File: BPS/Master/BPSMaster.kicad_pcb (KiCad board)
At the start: 2 copper layers, 100 x 75 mm, 180 parts, among them J1 SWD, J10 DisplayJumper, J11 FrontFans, J12 BackFans, J13 ErrorLightConnector, J14 Conn_01x03, J2 Logic Analyzer, J3 CurrentSlaveConnector, J4 CarPowerConnector, J5 CAN_Out, J6 ContactorConnector, J7 VoltageSlaveConnector, J8 DisplayConnector, J9 TempSlaveConnector, Q1 VND5N07-E, Q2 NVR4003NT3G, Q3 NVR4003NT3G, Q4 NVR4003NT3G, SW1 B3SL-1002P, U1 STM32F413RHTx, U10 LTC6820, U11 HX1188FNL, U12 LTC6820, U13 Si8641EC-B-IS1, U14 SI8660EC-B-IS1, U15 RI3-1205S, U16 SI8261ABC-IS, U2 RI3-1205S, U3 NCP1117-3.3_SOT223, U4 CDSOT23-T24CAN, U5 ADM3055E, U6 BAS70-04, U7 SI8261ABC-IS, U8 M24128, Y1 NX8045GB-8.000M-STD-CSJ-1

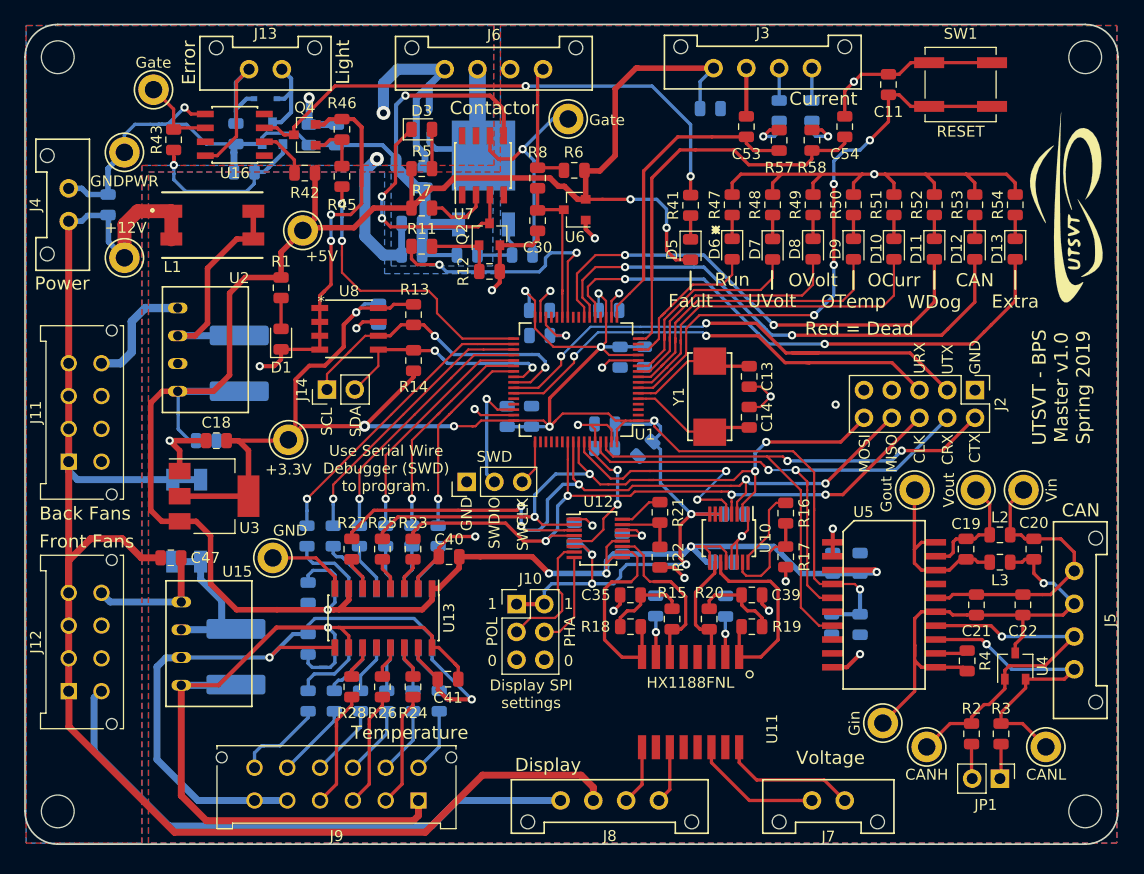
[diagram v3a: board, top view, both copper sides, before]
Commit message: Adds master board v1.1.
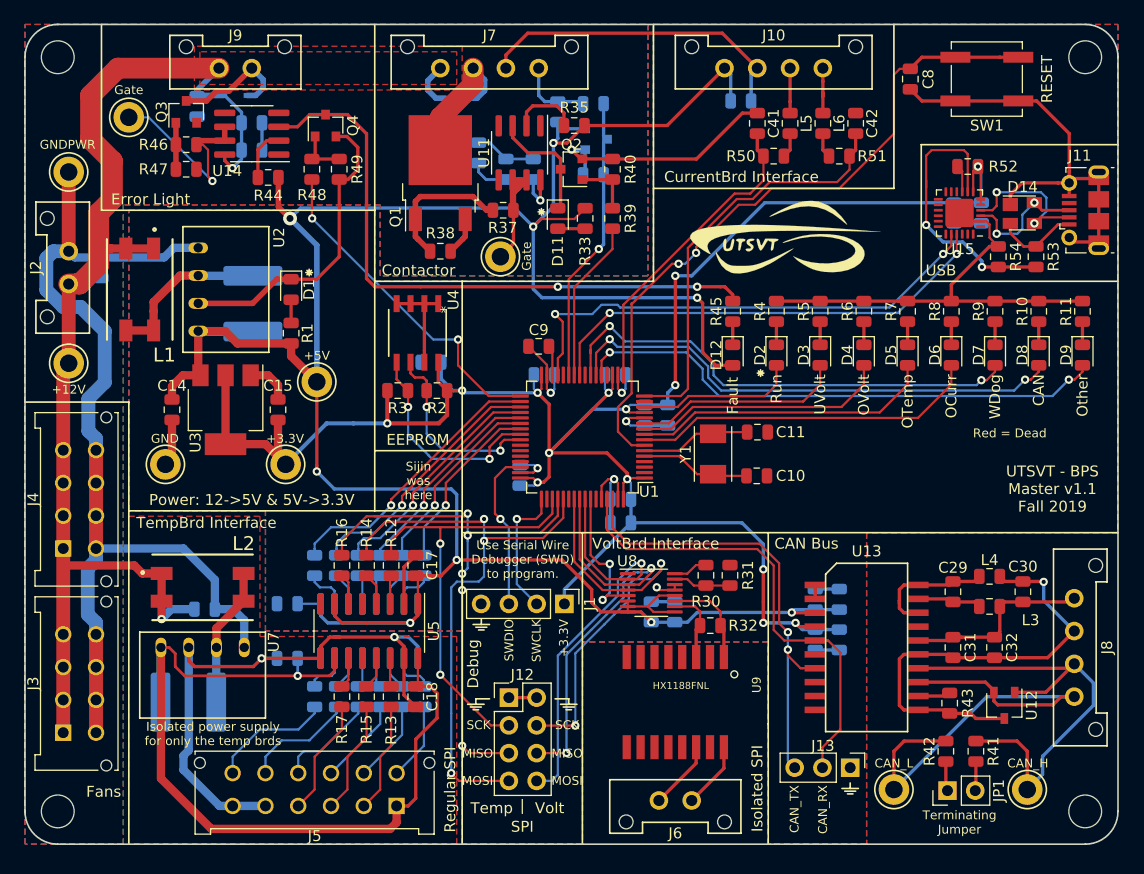
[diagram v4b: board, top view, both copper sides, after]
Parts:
- removed C45, C50: 0.1uF, Capacitor_SMD:C_0805_2012Metric
- removed C46: 470pF, Capacitor_SMD:C_2220_5650Metric
- removed C47: 4.7uF, Capacitor_SMD:C_0805_2012Metric
- removed C48, C53, C54: 1uF, Capacitor_SMD:C_0805_2012Metric
- removed C49: 10uF, Capacitor_SMD:C_0805_2012Metric
- removed J14: Conn_01x03, Connector_PinHeader_2.54mm:PinHeader_1x02_P2.54mm_Vertical
- removed R57, R58: 220k, Resistor_SMD:R_0805_2012Metric
- removed TP12: CAN_L, TestPoint:TestPoint_Keystone_5005-5009_Compact
- removed TP13: ContactorGate_TP, TestPoint:TestPoint_Keystone_5005-5009_Compact
- removed TP14: StrobeLightGate_TP, TestPoint:TestPoint_Keystone_5005-5009_Compact
- removed TP15: GNDPWR_TP, TestPoint:TestPoint_Keystone_5005-5009_Compact
- removed U16: SI8261ABC-IS, Package_SO:SOIC-8_3.9x4.9mm_P1.27mm
- added C32: 0.01uF, Capacitor_SMD:C_0805_2012Metric, F.Cu at (188.7, 132.0)
- added C33: 10uF, Capacitor_SMD:C_0805_2012Metric, B.Cu at (174.5, 127.6)
- added D14: SP0503BAHT, Package_TO_SOT_SMD:SOT-143, F.Cu at (191.2, 92.2)
- added U9: HX1188FNL, UTSVT_BPS:HXXXX, F.Cu at (159.5, 137.0)
- C10: value 1uF -> 6pF; moved to F.Cu
- C11: value 0.1uF -> 6pF
- C12: value 0.1uF -> 470pF; footprint Capacitor_SMD:C_0805_2012Metric -> Capacitor_SMD:C_2220_5650Metric
- C13: value 6pF -> 4.7uF; moved to B.Cu
- C14: value 6pF -> 10uF
- C15: value 470pF -> 10uF; footprint Capacitor_SMD:C_2220_5650Metric -> Capacitor_SMD:C_0805_2012Metric; moved to F.Cu
- C16: value 4.7uF -> 0.1uF
- C17: value 0.1uF -> 0.1u; moved to F.Cu
- C18: value 10uF -> 0.1u
- C19: value 10uF -> 0.1u; moved to B.Cu
- C20: value 0.22uF -> 0.1u; moved to B.Cu
- C21: value 0.1uF -> 470p; footprint Capacitor_SMD:C_0805_2012Metric -> Capacitor_SMD:C_2220_5650Metric; moved to B.Cu
- C22: value 0.01uF -> 4.7u; moved to B.Cu
- C23: value 10uF -> 0.1uF
- C25: value 0.1uF -> 1u
- C26: value 0.01uF -> 10u
- C27: value 1uF -> 0.1u
- C28: value 10uF -> 1u
- C29: value 0.1uF -> 0.22uF; moved to F.Cu
- C30: value 1uF -> 10uF
- C31, L5, L6, Q1: moved to F.Cu
- C34: value 0.01uF -> 0.1uF
- C35, C39: value 0.01uF -> 0.1uF; moved to B.Cu
- C36: value 0.1uF -> 0.01uF
- C37: value 0.01uF -> 1uF
- C38: value 0.1uF -> 10uF
- C40, R23, R24, R25, R26, R27, R28: moved to B.Cu
- C41: value 0.1uF -> 1uF
- C42: value 0.1uF -> 1uF; moved to F.Cu
- C43, C5: value 0.1uF -> 4.7uF
- C7: value 4.7uF -> 1uF
- C8: value 2.2uF -> 0.1uF; moved to F.Cu
- C9: value 0.1uF -> 2.2uF; moved to F.Cu
- D10: value OCurr -> 1N4148WS; footprint LED_SMD:LED_0805_2012Metric -> Diode_SMD:D_SOD-323; moved to B.Cu
- D11: value WDError -> ContactorEn
- D12: value CANError -> Fault
- D13: value Extra -> 1N4148WS; footprint LED_SMD:LED_0805_2012Metric -> Diode_SMD:D_SOD-323; moved to B.Cu
- D2: value 1N4148WS -> Heartbeat; footprint Diode_SMD:D_SOD-323 -> LED_SMD:LED_0805_2012Metric; moved to F.Cu
- D3: value ContactorEn -> UVolt
- D4: value 1N4148WS -> OVolt; footprint Diode_SMD:D_SOD-323 -> LED_SMD:LED_0805_2012Metric; moved to F.Cu
- D5: value Fault -> OTemp
- D6: value Heartbeat -> OCurr
- D7: value UVolt -> WDError
- D8: value OVolt -> CANError
- D9: value OTemp -> Extra
- J1: footprint Connector_PinHeader_2.54mm:PinHeader_1x03_P2.54mm_Vertical -> Connector_PinHeader_2.54mm:PinHeader_1x04_P2.54mm_Vertical
- J10: value DisplayJumper -> CurrentSlaveConnector; footprint Connector_PinHeader_2.54mm:PinHeader_2x03_P2.54mm_Vertical -> UTSVT_Connectors:Molex_MicroFit3.0_1x4xP3.00mm_PolarizingPeg_Vertical
- J11: value FrontFans -> USB_B_Micro; footprint UTSVT_Connectors:Molex_MicroFit3.0_2x4xP3.00mm_PolarizingPeg_Vertical -> Connector_USB:USB_Micro-B_Molex-105017-0001
- J12: value BackFans -> Logic Analyzer; footprint UTSVT_Connectors:Molex_MicroFit3.0_2x4xP3.00mm_PolarizingPeg_Vertical -> Connector_PinHeader_2.54mm:PinHeader_2x04_P2.54mm_Vertical
- J13: value ErrorLightConnector -> CAN Analyzer; footprint UTSVT_Connectors:Molex_MicroFit3.0_1x2xP3.00mm_PolarizingPeg_Vertical -> Connector_PinHeader_2.54mm:PinHeader_1x03_P2.54mm_Vertical
- J2: value Logic Analyzer -> CarPowerConnector; footprint Connector_PinHeader_2.54mm:PinHeader_2x05_P2.54mm_Vertical -> UTSVT_Connectors:Molex_MicroFit3.0_1x2xP3.00mm_PolarizingPeg_Vertical
- J3: value CurrentSlaveConnector -> FrontFans; footprint UTSVT_Connectors:Molex_MicroFit3.0_1x4xP3.00mm_PolarizingPeg_Vertical -> UTSVT_Connectors:Molex_MicroFit3.0_2x4xP3.00mm_PolarizingPeg_Vertical
- J4: value CarPowerConnector -> BackFans; footprint UTSVT_Connectors:Molex_MicroFit3.0_1x2xP3.00mm_PolarizingPeg_Vertical -> UTSVT_Connectors:Molex_MicroFit3.0_2x4xP3.00mm_PolarizingPeg_Vertical
- J5: value CAN_Out -> TempSlaveConnector; footprint UTSVT_Connectors:Molex_MicroFit3.0_1x4xP3.00mm_PolarizingPeg_Vertical -> UTSVT_Connectors:Molex_MicroFit3.0_2x6xP3.00mm_PolarizingPeg_Vertical
- J6: value ContactorConnector -> VoltageSlaveConnector; footprint UTSVT_Connectors:Molex_MicroFit3.0_1x4xP3.00mm_PolarizingPeg_Vertical -> UTSVT_Connectors:Molex_MicroFit3.0_1x2xP3.00mm_PolarizingPeg_Vertical
- J7: value VoltageSlaveConnector -> ContactorConnector; footprint UTSVT_Connectors:Molex_MicroFit3.0_1x2xP3.00mm_PolarizingPeg_Vertical -> UTSVT_Connectors:Molex_MicroFit3.0_1x4xP3.00mm_PolarizingPeg_Vertical
- J8: value DisplayConnector -> CAN_Out
- J9: value TempSlaveConnector -> ErrorLightConnector; footprint UTSVT_Connectors:Molex_MicroFit3.0_2x6xP3.00mm_PolarizingPeg_Vertical -> UTSVT_Connectors:Molex_MicroFit3.0_1x2xP3.00mm_PolarizingPeg_Vertical
- L2: value 2kH -> 10u; footprint Inductor_SMD:L_0805_2012Metric -> UTSVT_BPS:SRF0905A
- L4: value 10uH -> 2kH; footprint UTSVT_BPS:SRF0905A -> Inductor_SMD:L_0805_2012Metric; moved to F.Cu
- Q2, Q4: value NVR4003NT3G -> NTR4003NT1G
- Q3: value NVR4003NT3G -> NTR4003NT1G; moved to F.Cu
- R10: value 100k -> 750; moved to F.Cu
- R11: value 0 -> 750
- R12: value 100k -> 50
- R13, R14: value 4.7k -> 50
- R15: value 49.9 -> 50
- R16: value 806 -> 50
- R17: value 1.21k -> 50
- R18, R19, R20: value 49.9 -> 50; moved to B.Cu
- R2, R3: value 60 -> 4.7k
- R21: value 806 -> 50; moved to B.Cu
- R22: value 1.21k -> 50; moved to B.Cu
- R30: value 50 -> 806; moved to F.Cu
- R31: value 50 -> 1.21k; moved to F.Cu
- R32: value 50 -> 120; moved to F.Cu
- R33: value 50 -> 1.5k; moved to F.Cu
- R34: value 50 -> 4.7k
- R35: value 50 -> 470; moved to F.Cu
- R36: value 50 -> 1k
- R37, R39: value 50 -> 0; moved to F.Cu
- R38, R40: value 50 -> 10k; moved to F.Cu
- R4: value 0 -> 680
- R41: value 1.6k -> 60
- R42: value 470 -> 60
- R44: value 100k -> 470; moved to F.Cu
- R45: value 0 -> 1.6k
- R46: value 100k -> 0
- R47: value 680 -> 10k
- R48: value 750 -> 0
- R49: value 750 -> 10k
- R5: value 1.5k -> 750
- R50, R51: value 750 -> 220k
- R52: value 750 -> 1k
- R53: value 750 -> 22.1k
- R54: value 750 -> 47.5k
- R6: value 4.7k -> 750
- R7: value 470 -> 750
- R8: value 1k -> 750
- R9: value 0 -> 750; moved to F.Cu
- TP3: value GND_TP -> GNDPWR_TP
- TP4: value +3.3V_TP -> GND_TP
- TP5: value CAN_ISO_Vout -> +3.3V_TP
- TP6: value CAN_ISO_Vin -> ContactorGate_TP
- TP7: value CAN_ISO_GndIn -> CAN_H
- TP8: value CAN_ISO_GndOut -> CAN_L
- TP9: value CAN_H -> StrobeLightGate_TP
- U10: value LTC6820 -> BAS70-04; footprint Package_SO:MSOP-16_3x4mm_P0.5mm -> Package_TO_SOT_SMD:SOT-23; moved to B.Cu
- U11: value HX1188FNL -> SI8261ABC-IS; footprint UTSVT_BPS:HXXXX -> Package_SO:SOIC-8_3.9x4.9mm_P1.27mm
- U12: value LTC6820 -> CDSOT23-T24CAN; footprint Package_SO:MSOP-16_3x4mm_P0.5mm -> Package_TO_SOT_SMD:SOT-23W
- U13: value Si8641EC-B-IS1 -> ADM3055E; footprint Package_SO:SOIC-16_3.9x9.9mm_P1.27mm -> UTSVT_ICs:SOIC-20W_7.5x15.4mm_Pitch1.27mm
- U14: value SI8660EC-B-IS1 -> SI8261ABC-IS; footprint Package_SO:SOIC-16_3.9x9.9mm_P1.27mm -> Package_SO:SOIC-8_3.9x4.9mm_P1.27mm; moved to F.Cu
- U15: value RI3-1205S -> CP2102N-A01-GQFN24; footprint UTSVT_ICs:RI3_DC_Converter -> Package_DFN_QFN:QFN-24-1EP_4x4mm_P0.5mm_EP2.6x2.6mm
- U4: value CDSOT23-T24CAN -> M24128; footprint Package_TO_SOT_SMD:SOT-23W -> UTSVT_BPS:M24128-BRMN6P
- U5: value ADM3055E -> Si8641EC-B-IS1; footprint UTSVT_ICs:SOIC-20W_7.5x15.4mm_Pitch1.27mm -> Package_SO:SOIC-16_3.9x9.9mm_P1.27mm
- U6: value BAS70-04 -> SI8660EC-B-IS1; footprint Package_TO_SOT_SMD:SOT-23 -> Package_SO:SOIC-16_3.9x9.9mm_P1.27mm; moved to B.Cu
- U7: value SI8261ABC-IS -> RI3-1205S; footprint Package_SO:SOIC-8_3.9x4.9mm_P1.27mm -> UTSVT_ICs:RI3_DC_Converter
- U8: value M24128 -> LTC6820; footprint UTSVT_BPS:M24128-BRMN6P -> Package_SO:MSOP-16_3x4mm_P0.5mm
- Y1: value NX8045GB-8.000M-STD-CSJ-1 -> 8M; footprint UTSVT_BPS:NX8045GB-8.000M-STD-CSJ-1 -> Crystal:Crystal_SMD_TXC_7A-2Pin_5x3.2mm
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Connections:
- C10 pad 1: +3V3 -> /OSC_IN
- C11 pad 1: /NRST -> /OSC_OUT
- C12 pad 1: GND -> Net-(C12-Pad1)
- C13 pad 1: /OSC_OUT -> +12V
- C13 pad 2: GND -> GNDPWR
- C14 pad 1: /OSC_IN -> +5V
- C15 pad 1: Net-(C15-Pad1) -> +3V3
- C15 pad 2: +5V -> GND
- C16 pad 1: +12V -> +3V3
- C16 pad 2: GNDPWR -> GND
- C18 pad 1: +3V3 -> +5VL
- C18 pad 2: GND -> GND_A
- C19 pad 1: Net-(C19-Pad1) -> +5V
- C19 pad 2: Net-(C19-Pad2) -> GND
- C20 pad 1: Net-(C20-Pad1) -> +5VL
- C20 pad 2: Net-(C20-Pad2) -> GND_A
- C21 pad 1: Net-(C20-Pad1) -> Net-(C21-Pad1)
- C21 pad 2: Net-(C20-Pad2) -> +5VL
- C22 pad 1: Net-(C20-Pad1) -> +12V
- C22 pad 2: Net-(C20-Pad2) -> GNDPWR
- C25 pad 1: +3V3 -> GNDPWR
- C25 pad 2: GND -> +12V
- C26 pad 1: +3V3 -> +12V
- C26 pad 2: GND -> GNDPWR
- C27 pad 1: GNDPWR -> +12V
- C27 pad 2: +12V -> GNDPWR
- C28 pad 1: +12V -> /PB1
- C28 pad 2: GNDPWR -> GND
- C29 pad 1: +12V -> Net-(C29-Pad1)
- C29 pad 2: GNDPWR -> Net-(C29-Pad2)
- C30 pad 1: /PB1 -> Net-(C30-Pad1)
- C30 pad 2: GND -> Net-(C30-Pad2)
- C31 pad 1: +3V3 -> Net-(C30-Pad1)
- C31 pad 2: GND -> Net-(C30-Pad2)
- C34 pad 1: Net-(C34-Pad1) -> +5V
- C35 pad 1: Net-(C35-Pad1) -> +3V3
- C37 pad 1: Net-(C37-Pad1) -> GNDPWR
- C37 pad 2: GND -> +12V
- C38 pad 1: +5V -> +12V
- C38 pad 2: GND -> GNDPWR
- C39 pad 1: Net-(C39-Pad1) -> +12V
- C39 pad 2: GND -> GNDPWR
- C40 pad 1: +5V -> GND
- C40 pad 2: GND -> +5V
- C41 pad 1: +5VL -> /ADC1_CH3
- C41 pad 2: GND_A -> GND
- C42 pad 1: +3V3 -> /ADC1_CH2
- C43 pad 1: +5V -> +3V3
- C44 pad 1: +5V -> +3V3
- C8 pad 1: Net-(C8-Pad1) -> /NRST
- C9 pad 1: +3V3 -> Net-(C9-Pad1)
- D10 pad 1: Net-(D10-Pad1) -> +12V
- D10 pad 2: /PC0 -> /Contactor Driver/CONTACTOR_V-
- D11 pad 2: /PA7 -> Net-(D11-Pad2)
- D12 pad 2: /PA6 -> +5V
- D13 pad 1: Net-(D13-Pad1) -> +12V
- D13 pad 2: /PA5 -> Net-(D13-Pad2)
- D2 pad 1: +12V -> Net-(D2-Pad1)
- D2 pad 2: /Contactor Driver/CONTACTOR_V- -> /RUN
- D3 pad 2: Net-(D3-Pad2) -> /PC3
- D4 pad 1: +12V -> Net-(D4-Pad1)
- D4 pad 2: Net-(D4-Pad2) -> /PC2
- D5 pad 2: +5V -> /PC1
- D6 pad 2: /RUN -> /PC0
- D7 pad 2: /PC3 -> /PA7
- D8 pad 2: /PC2 -> /PA6
- D9 pad 2: /PC1 -> /PA5
- J1 pad 1: GND -> +3V3
- J1 pad 2: /SWDIO -> /SWCLK
- J1 pad 3: /SWCLK -> /SWDIO
- J10 pad 1: +3V3 -> +5V
- J10 pad 2: +3V3 -> GND
- J10 pad 3: /SPI/DISP_POL -> Net-(J10-Pad3)
- J10 pad 4: /SPI/DISP_PHA -> Net-(J10-Pad4)
- J11 pad 1: +12V -> Net-(D14-Pad2)
- J11 pad 2: +12V -> Net-(D14-Pad3)
- J11 pad 3: +12V -> Net-(D14-Pad4)
- J11 pad 4: +12V -> (no net)
- J11 pad 5: GNDPWR -> GND
- J11 pad 6: GNDPWR -> GND
- J12 pad 1: +12V -> GND
- J12 pad 2: +12V -> GND
- J12 pad 3: +12V -> /SPI3_CLK
- J12 pad 4: +12V -> /SPI1_CLK
- J12 pad 5: GNDPWR -> /SPI3_MISO
- J12 pad 6: GNDPWR -> /SPI1_MISO
- J12 pad 7: GNDPWR -> /SPI3_MOSI
- J12 pad 8: GNDPWR -> /SPI1_MOSI
- J13 pad 1: +12V -> GND
- J13 pad 2: Net-(D4-Pad2) -> /CAN1_RX
- J2 pad 1: GND -> +12V
- J2 pad 2: /CAN1_TX -> GNDPWR
- J3 pad 1: +5V -> +12V
- J3 pad 2: GND -> +12V
- J3 pad 3: Net-(J3-Pad3) -> +12V
- J3 pad 4: Net-(J3-Pad4) -> +12V
- J4 pad 2: GNDPWR -> +12V
- J5 pad 1: Net-(C20-Pad1) -> +5VL
- J5 pad 2: Net-(C20-Pad2) -> Net-(J5-Pad2)
- J5 pad 3: /CAN/CAN_H -> Net-(J5-Pad3)
- J5 pad 4: /CAN/CAN_L -> Net-(J5-Pad4)
- J6 pad 1: +12V -> Net-(J6-Pad1)
- J6 pad 2: /Contactor Driver/CONTACTOR_V- -> Net-(J6-Pad2)
- J7 pad 1: Net-(J7-Pad1) -> +12V
- J7 pad 2: Net-(J7-Pad2) -> /Contactor Driver/CONTACTOR_V-
- J8 pad 1: Net-(J8-Pad1) -> Net-(C30-Pad1)
- J8 pad 2: Net-(J8-Pad2) -> Net-(C30-Pad2)
- J8 pad 3: +12V -> /CAN/CAN_H
- J8 pad 4: GNDPWR -> /CAN/CAN_L
- J9 pad 1: +5VL -> +12V
- J9 pad 2: Net-(J9-Pad2) -> Net-(D13-Pad2)
- L1 pad 3: Net-(C15-Pad1) -> Net-(C12-Pad1)
- L1 pad 4: Net-(C15-Pad1) -> Net-(C12-Pad1)
- L2 pad 1: Net-(C20-Pad1) -> +12V
- L2 pad 2: Net-(C19-Pad1) -> +12V
- L3 pad 1: Net-(C20-Pad2) -> Net-(C30-Pad1)
- L3 pad 2: Net-(C19-Pad2) -> Net-(C29-Pad1)
- L4 pad 1: +12V -> Net-(C30-Pad2)
- L4 pad 2: +12V -> Net-(C29-Pad2)
- L5 pad 1: Net-(J3-Pad3) -> Net-(J10-Pad3)
- L6 pad 1: Net-(J3-Pad4) -> Net-(J10-Pad4)
- Q2 pad 3: Net-(D3-Pad1) -> Net-(D11-Pad1)
- Q3 pad 3: Net-(D4-Pad2) -> Net-(D13-Pad2)
- R10 pad 1: Net-(Q1-Pad1) -> Net-(D8-Pad1)
- R10 pad 2: GNDPWR -> GND
- R11 pad 1: Net-(Q2-Pad1) -> Net-(D9-Pad1)
- R11 pad 2: /PB0 -> GND
- R12 pad 1: Net-(Q2-Pad1) -> Net-(R12-Pad1)
- R12 pad 2: GND -> /SPI3_CLK
- R13 pad 1: +3V3 -> Net-(R13-Pad1)
- R13 pad 2: /I2C3_SCL -> Net-(J5-Pad2)
- R14 pad 1: +3V3 -> Net-(R14-Pad1)
- R14 pad 2: /I2C3_SDA -> /SPI3_MOSI
- R15 pad 1: /SPI/DISP_IP -> Net-(R15-Pad1)
- R15 pad 2: Net-(C35-Pad1) -> Net-(J5-Pad3)
- R16 pad 2: Net-(R16-Pad2) -> /SPI3_MISO
- R17 pad 1: GND -> Net-(R17-Pad1)
- R17 pad 2: Net-(R16-Pad1) -> Net-(J5-Pad4)
- R18 pad 1: /SPI/DISP_IM -> /TEMP_CS1
- R18 pad 2: Net-(C35-Pad1) -> Net-(R18-Pad2)
- R19 pad 1: /SPI/VOLT_IP -> /Temperature Board Interface/CS1
- R19 pad 2: Net-(C39-Pad1) -> Net-(R19-Pad2)
- R2 pad 1: /CAN/TERM_H -> +3V3
- R2 pad 2: /CAN/CAN_H -> /I2C3_SCL
- R20 pad 1: /SPI/VOLT_IM -> /TEMP_CS2
- R20 pad 2: Net-(C39-Pad1) -> Net-(R20-Pad2)
- R21 pad 1: Net-(R21-Pad1) -> /Temperature Board Interface/CS2
- R22 pad 1: GND -> /TEMP_CS3
- R22 pad 2: Net-(R21-Pad1) -> Net-(R22-Pad2)
- R23 pad 1: Net-(R23-Pad1) -> /Temperature Board Interface/CS3
- R23 pad 2: /SPI1_CLK -> Net-(R23-Pad2)
- R24 pad 1: Net-(R24-Pad1) -> /TEMP_CS4
- R24 pad 2: Net-(J9-Pad2) -> Net-(R24-Pad2)
- R25 pad 1: Net-(R25-Pad1) -> /Temperature Board Interface/CS4
- R25 pad 2: /SPI1_MOSI -> Net-(R25-Pad2)
- R26 pad 1: Net-(R26-Pad1) -> /TEMP_CS5
- R26 pad 2: Net-(J9-Pad3) -> Net-(R26-Pad2)
- R27 pad 1: Net-(R27-Pad1) -> /Temperature Board Interface/CS5
- R27 pad 2: /SPI1_MISO -> Net-(R27-Pad2)
- R28 pad 1: Net-(R28-Pad1) -> /TEMP_CS6
- R28 pad 2: Net-(J9-Pad4) -> Net-(R28-Pad2)
- R29 pad 1: /TEMP_CS1 -> /Temperature Board Interface/CS6
- R3 pad 1: /CAN/TERM_L -> +3V3
- R3 pad 2: /CAN/CAN_L -> /I2C3_SDA
- R30 pad 1: /SPI/CS1 -> Net-(R30-Pad1)
- R31 pad 1: /TEMP_CS2 -> GND
- R31 pad 2: Net-(R31-Pad2) -> Net-(R30-Pad1)
- R32 pad 1: /SPI/CS2 -> /Voltage Board Interface/VOLT_IP
- R32 pad 2: Net-(R32-Pad2) -> /Voltage Board Interface/VOLT_IM
- R33 pad 1: /TEMP_CS3 -> +5V
- R33 pad 2: Net-(R33-Pad2) -> Net-(D11-Pad2)
- R34 pad 1: /SPI/CS3 -> Net-(J7-Pad4)
- R34 pad 2: Net-(R34-Pad2) -> +5V
- R35 pad 1: /TEMP_CS4 -> Net-(R35-Pad1)
- R35 pad 2: Net-(R35-Pad2) -> +5V
- R36 pad 1: /SPI/CS4 -> /PB1
- R36 pad 2: Net-(R36-Pad2) -> Net-(J7-Pad4)
- R37 pad 1: /TEMP_CS5 -> Net-(Q1-Pad1)
- R38 pad 1: /SPI/CS5 -> Net-(Q1-Pad1)
- R38 pad 2: Net-(R38-Pad2) -> GNDPWR
- R39 pad 1: /TEMP_CS6 -> Net-(Q2-Pad1)
- R39 pad 2: Net-(R39-Pad2) -> /PB0
- R4 pad 1: /CAN/RSlope -> Net-(D2-Pad1)
- R4 pad 2: Net-(C20-Pad2) -> GND
- R40 pad 1: /SPI/CS6 -> Net-(Q2-Pad1)
- R40 pad 2: Net-(R40-Pad2) -> GND
- R41 pad 1: Net-(D5-Pad1) -> /CAN/TERM_H
- R41 pad 2: Net-(Q4-Pad3) -> /CAN/CAN_H
- R42 pad 1: Net-(R42-Pad1) -> /CAN/TERM_L
- R42 pad 2: +5V -> /CAN/CAN_L
- R43 pad 1: Net-(Q3-Pad1) -> /CAN/RSlope
- R43 pad 2: Net-(R43-Pad2) -> Net-(C30-Pad2)
- R44 pad 1: Net-(Q3-Pad1) -> Net-(R44-Pad1)
- R44 pad 2: GNDPWR -> +5V
- R45 pad 1: Net-(Q4-Pad1) -> Net-(D12-Pad1)
- R45 pad 2: /FAULT -> Net-(Q4-Pad3)
- R46 pad 1: Net-(Q4-Pad1) -> Net-(Q3-Pad1)
- R46 pad 2: GND -> Net-(R46-Pad2)
- R47 pad 1: Net-(D6-Pad1) -> Net-(Q3-Pad1)
- R47 pad 2: GND -> GNDPWR
- R48 pad 1: Net-(D7-Pad1) -> Net-(Q4-Pad1)
- R48 pad 2: GND -> /FAULT
- R49 pad 1: Net-(D8-Pad1) -> Net-(Q4-Pad1)
- R5 pad 1: +5V -> Net-(D3-Pad1)
- R5 pad 2: Net-(D3-Pad2) -> GND
- R50 pad 1: Net-(D9-Pad1) -> Net-(L5-Pad2)
- R50 pad 2: GND -> /ADC1_CH3
- R51 pad 1: Net-(D10-Pad1) -> Net-(L6-Pad2)
- R51 pad 2: GND -> /ADC1_CH2
- R52 pad 1: Net-(D11-Pad1) -> +3V3
- R52 pad 2: GND -> Net-(R52-Pad2)
- R53 pad 1: Net-(D12-Pad1) -> Net-(R53-Pad1)
- R53 pad 2: GND -> Net-(D14-Pad2)
- R54 pad 1: Net-(D13-Pad1) -> Net-(R53-Pad1)
- R6 pad 1: Net-(J6-Pad4) -> Net-(D4-Pad1)
- R6 pad 2: +5V -> GND
- R7 pad 1: Net-(R7-Pad1) -> Net-(D5-Pad1)
- R7 pad 2: +5V -> GND
- R8 pad 1: /PB1 -> Net-(D6-Pad1)
- R8 pad 2: Net-(J6-Pad4) -> GND
- R9 pad 1: Net-(Q1-Pad1) -> Net-(D7-Pad1)
- R9 pad 2: Net-(R9-Pad2) -> GND
- TP3 pad 1: GND -> GNDPWR
- TP4 pad 1: +3V3 -> GND
- TP5 pad 1: Net-(C19-Pad1) -> +3V3
- TP6 pad 1: Net-(C20-Pad1) -> Net-(R37-Pad2)
- TP7 pad 1: Net-(C20-Pad2) -> /CAN/CAN_H
- TP8 pad 1: Net-(C19-Pad2) -> /CAN/CAN_L
- TP9 pad 1: /CAN/CAN_H -> Net-(R46-Pad2)
- U1 pad 15: Net-(U1-Pad15) -> (no net)
- U1 pad 2: Net-(U1-Pad2) -> (no net)
- U1 pad 20: Net-(U1-Pad20) -> (no net)
- U1 pad 24: /PC4 -> (no net)
- U1 pad 25: /PC5 -> /USART3_RX
- U1 pad 28: Net-(U1-Pad28) -> (no net)
- U1 pad 29: Net-(U1-Pad29) -> /USART3_TX
- U1 pad 3: Net-(U1-Pad3) -> (no net)
- U1 pad 30: Net-(C8-Pad1) -> Net-(C9-Pad1)
- U1 pad 4: Net-(U1-Pad4) -> (no net)
- U1 pad 42: /UART1_TX -> (no net)
- U1 pad 43: /UART1_RX -> (no net)
- U1 pad 44: Net-(U1-Pad44) -> (no net)
- U1 pad 45: Net-(U1-Pad45) -> (no net)
- U1 pad 50: Net-(U1-Pad50) -> (no net)
- U1 pad 51: Net-(U1-Pad51) -> /SPI3_CLK
- U1 pad 52: Net-(U1-Pad52) -> /SPI3_MISO
- U1 pad 53: Net-(U1-Pad53) -> /SPI3_MOSI
- U1 pad 54: Net-(U1-Pad54) -> (no net)
- U1 pad 58: /LTC6811_CS -> /VOLT_CS
- U1 pad 59: /DISPLAY_CS -> (no net)
- U10 pad 2: /SPI1_MOSI -> +5V
- U10 pad 3: /SPI1_MISO -> /PB1
- U11 pad 1: /SPI/VOLT_IP -> (no net)
- U11 pad 2: Net-(C37-Pad1) -> Net-(R35-Pad1)
- U11 pad 3: /SPI/VOLT_IM -> Net-(D11-Pad1)
- U11 pad 5: (no net) -> GNDPWR
- U11 pad 6: /SPI/DISP_IP -> Net-(R37-Pad2)
- U11 pad 7: Net-(C34-Pad1) -> Net-(R37-Pad2)
- U11 pad 8: /SPI/DISP_IM -> +12V
- U12 pad 1: GND -> /CAN/CAN_H
- U12 pad 2: /SPI1_MOSI -> /CAN/CAN_L
- U12 pad 3: /SPI1_MISO -> Net-(C30-Pad2)
- U13 pad 1: +5V -> GND
- U13 pad 10: +5VL -> GND
- U13 pad 11: Net-(R28-Pad1) -> Net-(C30-Pad2)
- U13 pad 12: Net-(U13-Pad12) -> /CAN/RSlope
- U13 pad 13: Net-(R26-Pad1) -> /CAN/CAN_L
- U13 pad 14: Net-(R24-Pad1) -> /CAN/CAN_H
- U13 pad 15: GND_A -> Net-(C30-Pad2)
- U13 pad 16: +5VL -> Net-(C30-Pad1)
- U13 pad 3: Net-(R23-Pad1) -> +5V
- U13 pad 4: Net-(R25-Pad1) -> +3V3
- U13 pad 5: Net-(U13-Pad5) -> /CAN1_RX
- U13 pad 6: Net-(R27-Pad1) -> (no net)
- U13 pad 7: +5V -> /CAN1_TX
- U13 pad 8: GND -> (no net)
- U13 pad 9: GND_A -> (no net)
- U14 pad 1: +5V -> (no net)
- U14 pad 2: Net-(R29-Pad2) -> Net-(R44-Pad1)
- U14 pad 3: Net-(R31-Pad2) -> Net-(Q4-Pad3)
- U14 pad 4: Net-(R33-Pad2) -> (no net)
- U14 pad 5: Net-(R35-Pad2) -> GNDPWR
- U14 pad 6: Net-(R37-Pad2) -> Net-(R46-Pad2)
- U14 pad 7: Net-(R39-Pad2) -> Net-(R46-Pad2)
- U14 pad 8: GND -> +12V
- U15 pad 1: GNDPWR -> (no net)
- U15 pad 2: Net-(C46-Pad1) -> GND
- U15 pad 3: GND_A -> Net-(D14-Pad4)
- U15 pad 4: +5VL -> Net-(D14-Pad3)
- U2 pad 2: Net-(C15-Pad1) -> Net-(C12-Pad1)
- U4 pad 1: /CAN/CAN_H -> GND
- U4 pad 2: /CAN/CAN_L -> GND
- U4 pad 3: Net-(C20-Pad2) -> GND
- U5 pad 1: GND -> +5V
- U5 pad 10: GND -> +5VL
- U5 pad 11: Net-(C20-Pad2) -> Net-(R17-Pad1)
- U5 pad 12: /CAN/RSlope -> (no net)
- U5 pad 13: /CAN/CAN_L -> Net-(R15-Pad1)
- U5 pad 14: /CAN/CAN_H -> Net-(R13-Pad1)
- U5 pad 15: Net-(C20-Pad2) -> GND_A
- U5 pad 16: Net-(C20-Pad1) -> +5VL
- U5 pad 3: +5V -> Net-(R12-Pad1)
- U5 pad 4: +3V3 -> Net-(R14-Pad1)
- U5 pad 5: /CAN1_RX -> (no net)
- U5 pad 6: Net-(U5-Pad6) -> Net-(R16-Pad1)
- U5 pad 7: /CAN1_TX -> +5V
- U5 pad 8: Net-(U5-Pad8) -> GND
- U5 pad 9: Net-(U5-Pad9) -> GND_A
- U6 pad 1: GND -> +5V
- U6 pad 2: +5V -> Net-(R18-Pad2)
- U6 pad 3: /PB1 -> Net-(R20-Pad2)
- U7 pad 1: Net-(U7-Pad1) -> GNDPWR
- U7 pad 2: Net-(R7-Pad1) -> Net-(C21-Pad1)
- U7 pad 3: Net-(D3-Pad1) -> GND_A
- U7 pad 4: Net-(U7-Pad4) -> +5VL
- U8 pad 2: GND -> /SPI1_MOSI
- U8 pad 3: GND -> /SPI1_MISO
- U8 pad 4: GND -> /SPI1_CLK
- U8 pad 5: /I2C3_SDA -> /VOLT_CS
- U8 pad 6: /I2C3_SCL -> +5V
- U8 pad 7: GND -> +5V
- U8 pad 8: +3V3 -> +5V
- Y1 pad 1: /OSC_OUT -> /OSC_IN
- Y1 pad 2: /OSC_IN -> /OSC_OUT
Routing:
- net +12V: track 207.4 -> 146.1 mm
- net /SPI3_MOSI: track 0.00 -> 54.0 mm, vias 0 -> 3
- net GNDPWR: track 155.2 -> 102.1 mm, vias 2 -> 0
- net /SPI3_MISO: track 0.00 -> 50.9 mm, vias 0 -> 5
- net /UART1_TX: track 48.0 -> 0.00 mm, vias 2 -> 0
- net /USART3_TX: track 0.00 -> 46.2 mm, vias 0 -> 2
- net GND: track 183.2 -> 228.2 mm, vias 25 -> 7
- net Net-(C20-Pad2): track 44.6 -> 0.00 mm, vias 1 -> 0
- net /USART3_RX: track 0.00 -> 42.6 mm, vias 0 -> 2
- net /UART1_RX: track 42.2 -> 0.00 mm, vias 2 -> 0
- net Net-(C30-Pad2): track 0.00 -> 41.5 mm, vias 0 -> 1
- net /SPI3_CLK: track 0.00 -> 40.1 mm, vias 0 -> 2
- net /SPI1_MISO: track 71.9 -> 37.5 mm, vias 5 -> 2
- net /SPI1_MOSI: track 64.2 -> 37.5 mm, vias 4 -> 1
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- added copper zone on F.Cu, net GNDPWR
- added copper zone on F.Cu, net GND_A
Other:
- board text added: "+5Vcan"
- board text added: "+5Vcan is isolated from +5V"
- board text added: "+5Viso is isolated from +5V"
- board text added: "All caps on this side of the board are bypass capacitors"
- board text added: "CAN Bus"
- board text added: "CAN_H"
- board text added: "CAN_L"
- board text added: "CAN_RX"
- board text added: "CAN_TX"
- board text added: "CurrentBrd Interface"
- board text added: "Debug"
- board text added: "EEPROM"
- board text added: "Error Light"
- board text added: "Fans"
- board text added: "GNDcan"
- board text added: "Isolated SPI"
- board text added: "Isolated power supply for only the temp brds"
- board text added: "Other"
- board text added: "Power: 12->5V & 5V->3.3V"
- board text added: "Regular SPI"
- board text added: "SPI"
- board text added: "Sijin was here"
- board text added: "Temp"
- board text added: "TempBrd Interface"
- board text added: "Terminating Jumper"
- board text added: "USB"
- board text added: "UTSVT - BPS Master v1.1 Fall 2019"
- board text added: "Use PuTTY for CLI"
- board text added: "Volt"
- board text added: "VoltBrd Interface"
- board text added: "WARNING! GNDPWR and GND are isolated from each other"
- board text added: "|"
- board text removed: "0"
- board text removed: "Back Fans"
- board text removed: "CANH"
- board text removed: "CANL"
- board text removed: "CRX"
- board text removed: "CTX"
- board text removed: "Current"
- board text removed: "Display"
- board text removed: "Display SPI settings"
- board text removed: "Error"
- board text removed: "Extra"
- board text removed: "Front Fans"
- board text removed: "GNDiso"
- board text removed: "Gin"
- board text removed: "Gout"
- board text removed: "Light"
- board text removed: "PHA"
- board text removed: "POL"
- board text removed: "Power"
- board text removed: "SCL"
- board text removed: "SDA"
- board text removed: "SWD"
- board text removed: "Spring 2019: Monolo Alvarez Chase Block Corbin Capo Richard Li Austin Tsao Garrett Wong Sihyung Woo Sijin Woo"
- board text removed: "Temperature"
- board text removed: "URX"
- board text removed: "UTSVT - BPS Master v1.0 Spring 2019"
- board text removed: "UTX"
- board text removed: "Vin"
- board text removed: "Voltage"
- board text removed: "Vout"

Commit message: Edits master board to not have temperature board pinouts.
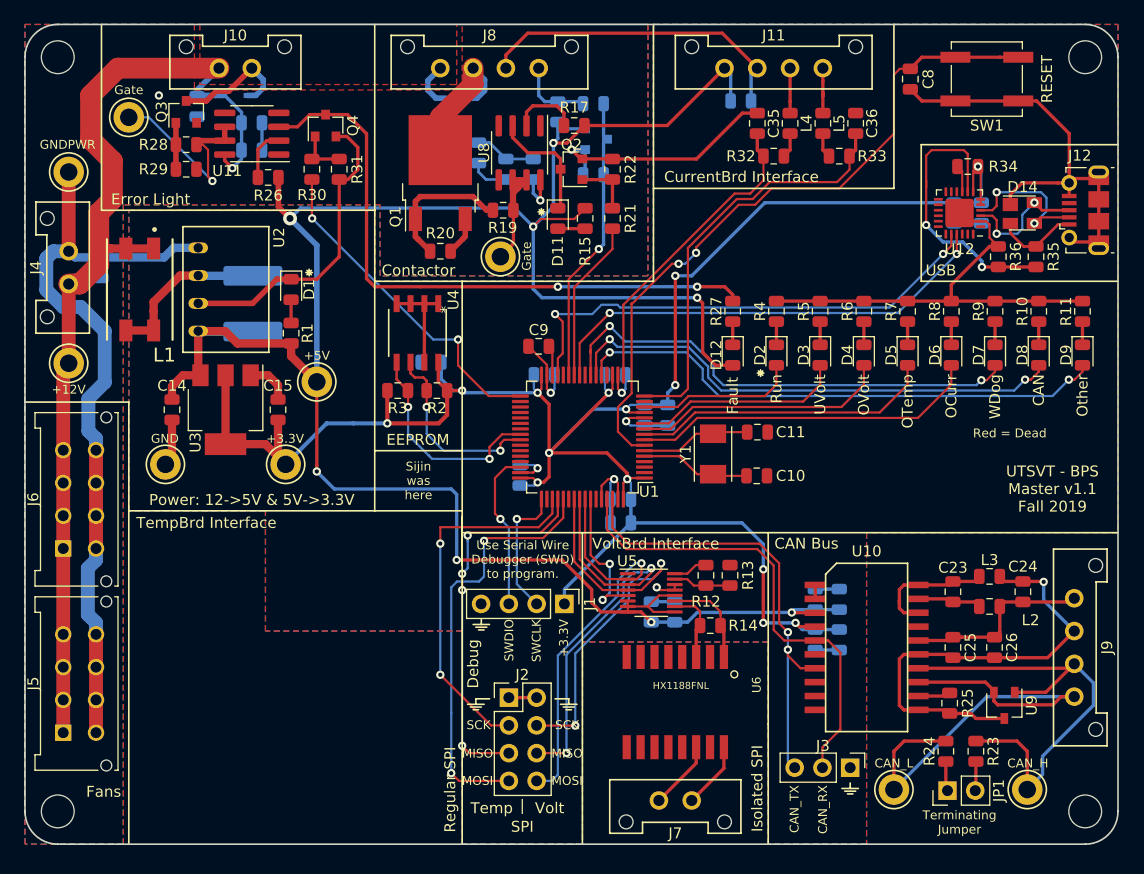
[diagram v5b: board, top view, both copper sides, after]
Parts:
- removed the C17 at (135.8, 124.5)
- removed the C18 at (135.8, 136.5)
- removed the C19 at (124.0, 128.0)
- removed the C20 at (124.0, 133.0)
- removed the C21 at (115.0, 137.0)
- removed the C22 at (116.4, 128.5)
- removed G***: LOGO, UTSVT_Special:Hallock_Image_Small
- removed G***: LOGO, UTSVT_Special:UTSVT_Logo_Symbol
- removed the J5 at (134.0, 146.5)
- removed the L2 at (116.2, 126.5)
- removed the R12 at (133.5, 124.5)
- removed the R13 at (133.5, 136.5)
- removed the R14 at (131.2, 124.5)
- removed the R15 at (131.2, 136.5)
- removed the R16 at (129.0, 124.5)
- removed the R17 at (129.0, 136.5)
- removed the R18 at (126.5, 124.5)
- removed the R19 at (126.5, 136.5)
- removed the R20 at (128.5, 124.5)
- removed the R21 at (128.5, 136.5)
- removed the R22 at (130.5, 124.5)
- removed the R23 at (130.5, 136.5)
- removed the R24 at (132.5, 124.5)
- removed the R25 at (132.5, 136.5)
- removed the R26 at (134.5, 124.5)
- removed the R27 at (134.5, 136.5)
- removed the R28 at (136.5, 124.5)
- removed the R29 at (136.5, 136.5)
- removed the U5 at (131.5, 130.5)
- removed the U6 at (131.5, 130.5)
- removed the U7 at (116.2, 132.0)
- C10, C11: value 6pF -> 10pF
- C9: value 2.2uF -> 4.7u
- renumbered C23 to C17, C24 to C18, C25 to C19, C26 to C20, C27 to C21, C28 to C22, C29 to C23, C30 to C24, C31 to C25, C32 to C26, C33 to C27, C34 to C28, C35 to C29, C36 to C30, C37 to C31, C38 to C32, C39 to C33, C40 to C34, C41 to C35, C42 to C36, C43 to C37, C44 to C38, J9 to J10, J10 to J11, J11 to J12, J12 to J2, J13 to J3, J2 to J4, J3 to J5, J4 to J6, J6 to J7, J7 to J8, J8 to J9, L3 to L2, L4 to L3, L5 to L4, L6 to L5, R30 to R12, R31 to R13, R32 to R14, R33 to R15, R34 to R16, R35 to R17, R36 to R18, R37 to R19, R38 to R20, R39 to R21, R40 to R22, R41 to R23, R42 to R24, R43 to R25, R44 to R26, R45 to R27, R46 to R28, R47 to R29, R48 to R30, R49 to R31, R50 to R32, R51 to R33, R52 to R34, R53 to R35, R54 to R36, U13 to U10, U14 to U11, U15 to U12, U8 to U5, U9 to U6, U10 to U7, U11 to U8, U12 to U9
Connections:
- U1 pad 34: /TEMP_CS1 -> (no net)
- U1 pad 35: /TEMP_CS2 -> (no net)
- U1 pad 36: /TEMP_CS3 -> (no net)
- U1 pad 37: /TEMP_CS4 -> (no net)
- U1 pad 38: /TEMP_CS5 -> (no net)
- U1 pad 39: /TEMP_CS6 -> (no net)
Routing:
- net +5VL: track 82.3 -> 0.00 mm, vias 1 -> 0
- net GND_A: track 55.0 -> 0.00 mm, vias 2 -> 0
- net +5V: track 246.1 -> 217.2 mm, vias 9 -> 8
- net /TEMP_CS1: track 25.6 -> 0.00 mm, vias 1 -> 0
- net /TEMP_CS2: track 23.6 -> 0.00 mm, vias 1 -> 0
- net /TEMP_CS3: track 21.5 -> 0.00 mm, vias 1 -> 0
- net GNDPWR: track 102.1 -> 81.7 mm, vias 0 -> 1
- net /TEMP_CS4: track 19.2 -> 0.00 mm, vias 1 -> 0
- net /TEMP_CS5: track 17.8 -> 0.00 mm, vias 1 -> 0
- net +12V: track 146.1 -> 128.4 mm, vias 3 -> 2
- net /SPI3_MISO: track 50.9 -> 34.5 mm, vias 5 -> 4
- net /TEMP_CS6: track 16.3 -> 0.00 mm, vias 1 -> 0
- net /SPI3_MOSI: track 54.0 -> 39.1 mm, vias 3 -> 2
- net Net-(C21-Pad1): track 12.8 -> 0.00 mm
- net /Temperature Board Interface/CS1: track 11.2 -> 0.00 mm
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- removed copper zone on F.Cu, net GND_A
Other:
- board text removed: "+5Viso"
- board text removed: "+5Viso is isolated from +5V"
- board text removed: "1"
- board text removed: "2"
- board text removed: "3"
- board text removed: "4"
- board text removed: "5"
- board text removed: "6"
- board text removed: "CLK"
- board text removed: "Isolated power supply for only the temp brds"

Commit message: Adds BPS master board with no temperature brd electronics and ContactorDriver for dashboard to control.
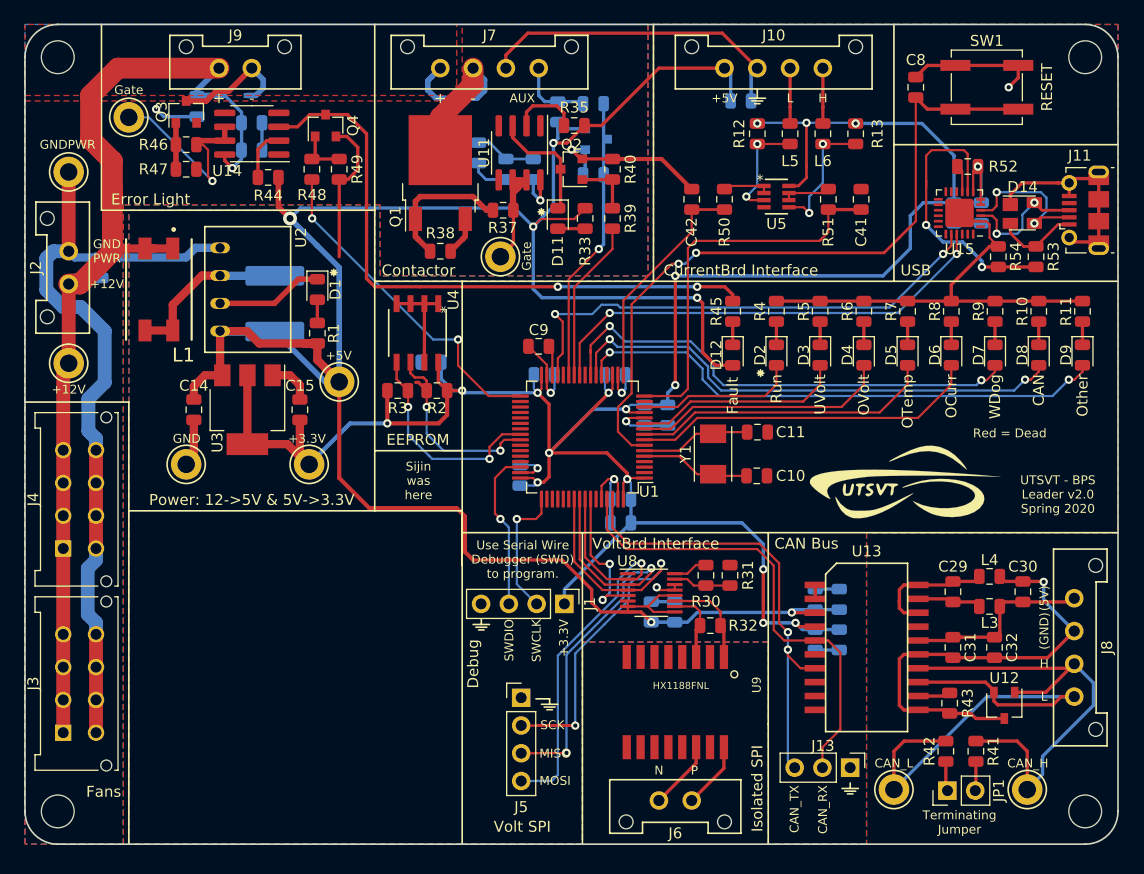
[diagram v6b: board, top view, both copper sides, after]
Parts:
- removed the C36 at (176.0, 84.0)
- removed the J2 at (144.3, 136.6)
- removed L2: 2kH, Inductor_SMD:L_0805_2012Metric
- added C42: 0.01u, Capacitor_SMD:C_0805_2012Metric, F.Cu at (161.0, 91.0)
- added G***: LOGO, UTSVT_Special:Hallock_Image_Small, B.Cu at (184.5, 109.0)
- added G***: LOGO, UTSVT_Special:UTSVT_Logo_Symbol, F.Cu at (180.2, 117.0)
- added J5: SPI Analyzer, Connector_PinHeader_2.54mm:PinHeader_1x04_P2.54mm_Vertical, F.Cu at (145.4, 136.6)
- added L3: 2kH, Inductor_SMD:L_0805_2012Metric, F.Cu at (188.2, 128.2)
- added R12: 100, Resistor_SMD:R_0805_2012Metric, F.Cu at (167.0, 85.0)
- added R13: 100, Resistor_SMD:R_0805_2012Metric, F.Cu at (176.0, 85.0)
- added U5: LTC6256, UTSVT_BPS:LTC6256CTS8-TRMPBF, F.Cu at (168.8, 90.8)
- C41: renamed from C35; value 1uF -> 0.01u
- R50: renamed from R32; value 220k -> 100
- R51: renamed from R33; value 220k -> 100
- moved C41 11.8 mm to (176.5, 91.0)
- moved R50 5.99 mm to (164.0, 91.0), turned to 270 degrees
- moved R51 4.07 mm to (173.5, 91.0), turned to 270 degrees
- moved D1 2.40 mm to (126.8, 99.2)
- moved R1 2.40 mm to (126.8, 103.2)
- moved TP5 2.15 mm to (126.0, 115.2)
- moved TP2 2.05 mm to (128.8, 107.7)
- moved C12 2.00 mm to (122.8, 100.5)
- moved C14 2.00 mm to (115.5, 110.2)
- moved C15 2.00 mm to (125.2, 110.2)
- moved U2 2.00 mm to (117.8, 99.2)
- moved U3 2.00 mm to (120.3, 110.2)
- moved TP4 1.90 mm to (114.8, 115.2)
- moved L1 1.75 mm to (112.2, 99.2)
- moved L5 0.95 mm to (170.0, 85.0)
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- renumbered C17 to C23, C18 to C24, C19 to C25, C20 to C26, C21 to C27, C22 to C28, C23 to C29, C24 to C30, C25 to C31, C26 to C32, C27 to C33, C28 to C34, C29 to C35, C30 to C36, C31 to C37, C32 to C38, C33 to C39, C34 to C40, C37 to C43, C38 to C44, J11 to J10, J12 to J11, J3 to J13, J4 to J2, J5 to J3, J6 to J4, J7 to J6, J8 to J7, J9 to J8, J10 to J9, L3 to L4, L4 to L5, L5 to L6, R12 to R30, R13 to R31, R14 to R32, R15 to R33, R16 to R34, R17 to R35, R18 to R36, R19 to R37, R20 to R38, R21 to R39, R22 to R40, R23 to R41, R24 to R42, R25 to R43, R26 to R44, R27 to R45, R28 to R46, R29 to R47, R30 to R48, R31 to R49, R34 to R52, R35 to R53, R36 to R54, U7 to U10, U8 to U11, U9 to U12, U10 to U13, U11 to U14, U12 to U15, U5 to U8, U6 to U9
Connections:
- C41 pad 1: /ADC1_CH3 -> /ADC1_CH2
- J11 pad 4: (no net) -> Net-(J11-Pad4)
- L5 pad 2: Net-(L4-Pad2) -> Net-(L5-Pad2)
- L6 pad 2: Net-(L5-Pad2) -> Net-(L6-Pad2)
- R50 pad 1: Net-(L4-Pad2) -> Net-(R50-Pad1)
- R51 pad 1: Net-(L5-Pad2) -> Net-(R51-Pad1)
- U1 pad 15: (no net) -> Net-(U1-Pad15)
- U1 pad 2: (no net) -> Net-(U1-Pad2)
- U1 pad 20: (no net) -> Net-(U1-Pad20)
- U1 pad 24: (no net) -> Net-(U1-Pad24)
- U1 pad 28: (no net) -> Net-(U1-Pad28)
- U1 pad 3: (no net) -> Net-(U1-Pad3)
- U1 pad 34: (no net) -> Net-(U1-Pad34)
- U1 pad 35: (no net) -> Net-(U1-Pad35)
- U1 pad 36: (no net) -> Net-(U1-Pad36)
- U1 pad 37: (no net) -> Net-(U1-Pad37)
- U1 pad 38: (no net) -> Net-(U1-Pad38)
- U1 pad 39: (no net) -> Net-(U1-Pad39)
- U1 pad 4: (no net) -> Net-(U1-Pad4)
- U1 pad 42: (no net) -> Net-(U1-Pad42)
- U1 pad 43: (no net) -> Net-(U1-Pad43)
- U1 pad 44: (no net) -> Net-(U1-Pad44)
- U1 pad 45: (no net) -> Net-(U1-Pad45)
- U1 pad 50: (no net) -> Net-(U1-Pad50)
- U1 pad 51: /SPI3_CLK -> Net-(U1-Pad51)
- U1 pad 52: /SPI3_MISO -> Net-(U1-Pad52)
- U1 pad 53: /SPI3_MOSI -> Net-(U1-Pad53)
- U1 pad 54: (no net) -> Net-(U1-Pad54)
- U1 pad 59: (no net) -> Net-(U1-Pad59)
- U11 pad 1: (no net) -> Net-(U11-Pad1)
- U11 pad 4: (no net) -> Net-(U11-Pad4)
- U13 pad 17: (no net) -> Net-(U13-Pad17)
- U13 pad 6: (no net) -> Net-(U13-Pad6)
- U13 pad 8: (no net) -> Net-(U13-Pad8)
- U13 pad 9: (no net) -> Net-(U13-Pad9)
- U14 pad 1: (no net) -> Net-(U14-Pad1)
- U14 pad 4: (no net) -> Net-(U14-Pad4)
- U15 pad 1: (no net) -> Net-(U15-Pad1)
- U15 pad 10: (no net) -> Net-(U15-Pad10)
- U15 pad 11: (no net) -> Net-(U15-Pad11)
- U15 pad 12: (no net) -> Net-(U15-Pad12)
- U15 pad 13: (no net) -> Net-(U15-Pad13)
- U15 pad 14: (no net) -> Net-(U15-Pad14)
- U15 pad 15: (no net) -> Net-(U15-Pad15)
- U15 pad 16: (no net) -> Net-(U15-Pad16)
- U15 pad 17: (no net) -> Net-(U15-Pad17)
- U15 pad 18: (no net) -> Net-(U15-Pad18)
- U15 pad 19: (no net) -> Net-(U15-Pad19)
- U15 pad 22: (no net) -> Net-(U15-Pad22)
- U15 pad 23: (no net) -> Net-(U15-Pad23)
- U15 pad 24: (no net) -> Net-(U15-Pad24)
- U9 pad 10: (no net) -> Net-(U9-Pad10)
- U9 pad 11: (no net) -> Net-(U9-Pad11)
- U9 pad 15: (no net) -> Net-(U9-Pad15)
- U9 pad 2: (no net) -> Net-(U9-Pad2)
- U9 pad 6: (no net) -> Net-(U9-Pad6)
- U9 pad 7: (no net) -> Net-(U9-Pad7)
- U9 pad 8: (no net) -> Net-(U9-Pad8)
- U9 pad 9: (no net) -> Net-(U9-Pad9)
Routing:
- net /SPI3_MOSI: track 39.1 -> 0.00 mm, vias 2 -> 0
- net /SPI3_MISO: track 34.5 -> 0.00 mm, vias 4 -> 0
- net /SPI3_CLK: track 33.8 -> 0.00 mm, vias 2 -> 0
- net +3V3: track 204.1 -> 234.2 mm, vias 14 -> 17
- net GND: track 223.3 -> 200.4 mm, vias 7 -> 8
- net Net-(L6-Pad2): track 0.00 -> 11.9 mm, vias 0 -> 2
- net /ADC1_CH3: track 28.5 -> 20.7 mm
- net Net-(L5-Pad2): track 2.30 -> 9.97 mm, vias 0 -> 2
- net +5V: track 217.2 -> 223.9 mm, vias 8 -> 6
- net GNDPWR: track 81.7 -> 87.8 mm
- net /SPI1_CLK: track 38.8 -> 43.7 mm
- net Net-(R51-Pad1): track 0.00 -> 4.74 mm
- net Net-(R50-Pad1): track 0.00 -> 4.38 mm
- net /ADC1_CH2: track 38.4 -> 35.9 mm
- net +12V: track 128.4 -> 130.9 mm
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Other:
- board text added: "(5V)"
- board text added: "(GND)"
- board text added: "GND PWR"
- board text added: "H"
- board text added: "L"
- board text added: "N"
- board text added: "P"
- board text added: "UTSVT - BPS Leader v2.0 Spring 2020"
- board text added: "Volt SPI"
- board text removed: "Regular SPI"
- board text removed: "SPI"
- board text removed: "Temp"
- board text removed: "TempBrd Interface"
- board text removed: "UTSVT - BPS Master v1.1 Fall 2019"
- board text removed: "Volt"
- board text removed: "|"
